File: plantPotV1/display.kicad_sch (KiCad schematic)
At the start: 1 part, among them J2 Conn_01x04_Socket

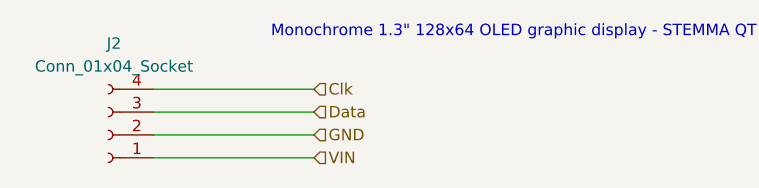
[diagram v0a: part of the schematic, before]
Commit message: changed to meet proposal
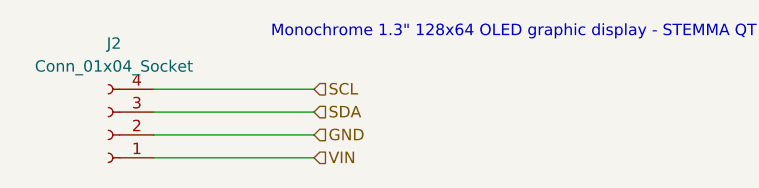
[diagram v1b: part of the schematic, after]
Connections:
- net Clk renamed SCL
- net Data renamed SDA
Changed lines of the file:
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@@
 		)
 	)
-	(hierarchical_label "Data"
+	(hierarchical_label "SDA"
 		(shape input)
 		(at 86.36 67.31 0)
@@
 		)
 	)
-	(hierarchical_label "Clk"
+	(hierarchical_label "SCL"
 		(shape input)
 		(at 86.36 64.77 0)

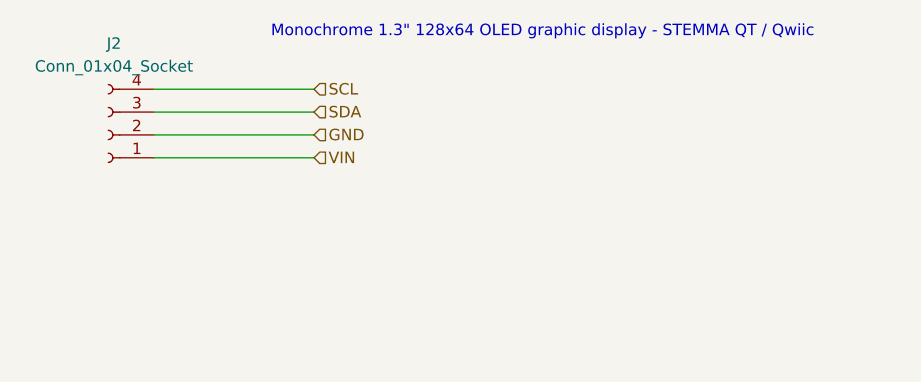
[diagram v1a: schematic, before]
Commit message: updated circuit diagram (top only)
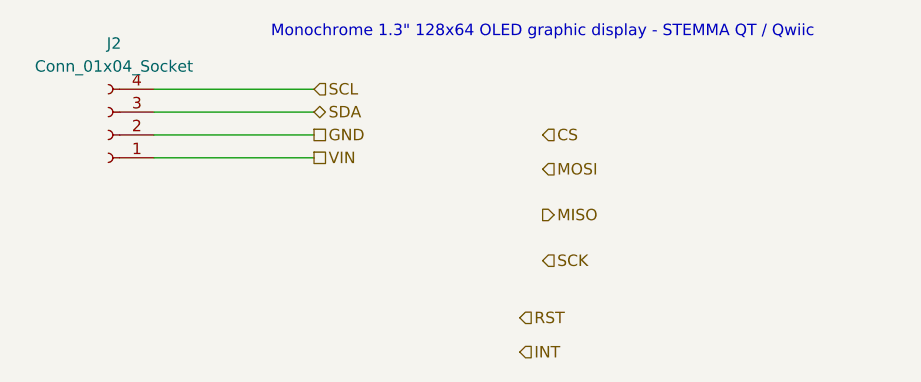
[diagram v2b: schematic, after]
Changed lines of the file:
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@@
+		)
+	)
+	(hierarchical_label "SCK"
+		(shape input)
+		(at 111.76 83.82 0)
+		(fields_autoplaced yes)
+		(effects
+			(font
+				(size 1.27 1.27)
+			)
+			(justify left)
+		)
+	)
+	(hierarchical_label "GND"
+		(shape passive)
+		(at 86.36 69.85 0)
+		(fields_autoplaced yes)
+		(effects
+			(font
+				(size 1.27 1.27)
+			)
+			(justify left)
+		)
+	)
+	(hierarchical_label "INT"
+		(shape input)
+		(at 109.22 93.98 0)
+		(fields_autoplaced yes)
+		(effects
+			(font
+				(size 1.27 1.27)
+			)
+			(justify left)
 		)
 	)
 	(hierarchical_label "SDA"
+		(shape bidirectional)
+		(at 86.36 67.31 0)
+		(fields_autoplaced yes)
+		(effects
+			(font
+				(size 1.27 1.27)
+			)
+			(justify left)
+		)
+	)
+	(hierarchical_label "MOSI"
 		(shape input)
-		(at 86.36 67.31 0)
+		(at 111.76 73.66 0)
+		(fields_autoplaced yes)
+		(effects
+			(font
+				(size 1.27 1.27)
+			)
+			(justify left)
+		)
+	)
+	(hierarchical_label "VIN"
+		(shape passive)
+		(at 86.36 72.39 0)
+		(fields_autoplaced yes)
+		(effects
+			(font
+				(size 1.27 1.27)
+			)
+			(justify left)
+		)
+	)
+	(hierarchical_label "RST"
+		(shape input)
+		(at 109.22 90.17 0)
+		(fields_autoplaced yes)
+		(effects
+			(font
+				(size 1.27 1.27)
+			)
+			(justify left)
+		)
+	)
+	(hierarchical_label "CS"
+		(shape input)
+		(at 111.76 69.85 0)
+		(fields_autoplaced yes)
+		(effects
+			(font
+				(size 1.27 1.27)
+			)
+			(justify left)
+		)
+	)
+	(hierarchical_label "MISO"
+		(shape output)
+		(at 111.76 78.74 0)
 		(fields_autoplaced yes)
 		(effects
@@
 		(fields_autoplaced yes)
 		(effects
-			(font
-				(size 1.27 1.27)
-			)
-			(justify left)
-		)
-	)
-	(hierarchical_label "GND"
-		(shape input)
-		(at 86.36 69.85 0)
-		(fields_autoplaced yes)
-		(effects
-			(font
-				(size 1.27 1.27)
-			)
-			(justify left)
-		)
-	)
-	(hierarchical_label "VIN"
-		(shape input)
-		(at 86.36 72.39 0)
-		(fields_autoplaced yes)
-		(effects
